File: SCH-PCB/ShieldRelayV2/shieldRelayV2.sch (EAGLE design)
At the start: 90 parts, among them IC1 LM2596SX-5.0_NOPB, IC2 LM1117MPX-33NOPB, IC3 FT231XS-R, K1 SLA-05VDC-SL-C, K2 SRD-05VDC-SL-C, K3 G3MB-202PL-DC5, K5 G3MB-202PL-DC5, K6 SRD-05VDC-SL-C, Q1 MMST2222A-7-F, Q2 MMST2222A-7-F, Q3 MMST2222A-7-F, Q4 MMST2222A-7-F, Q5 MMST2222A-7-F, Q6 MMBT3904-TP, Q7 MMBT3904-TP

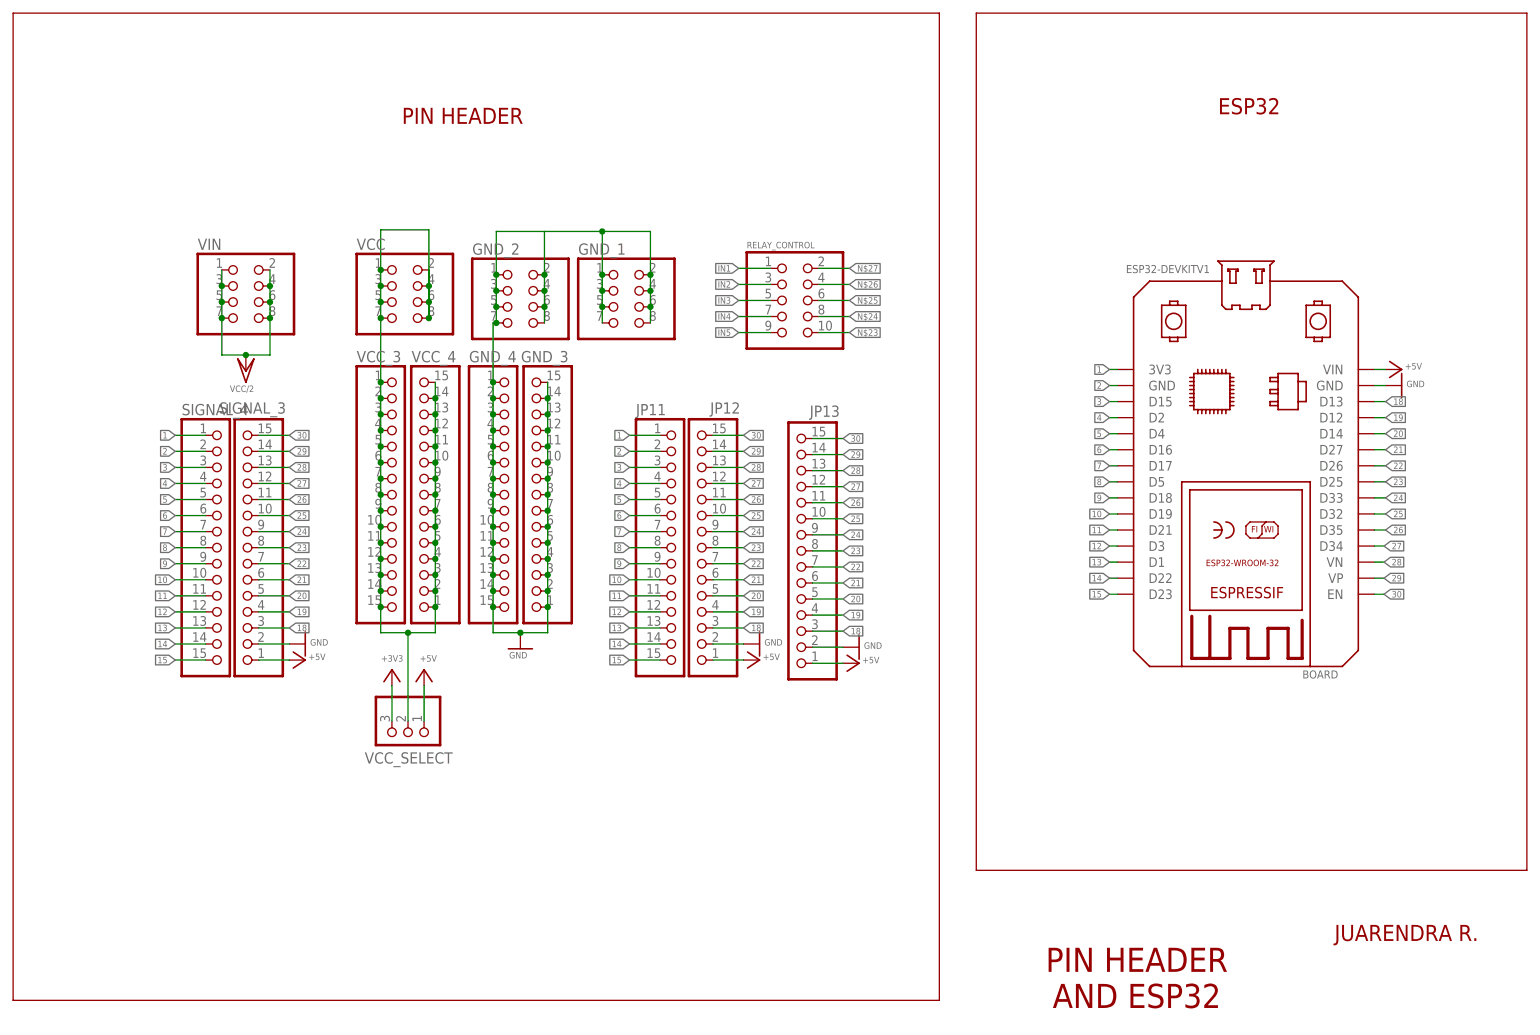
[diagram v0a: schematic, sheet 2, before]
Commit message: FEAT: update sch, board, gerber adn bom for esp embedded to pcb
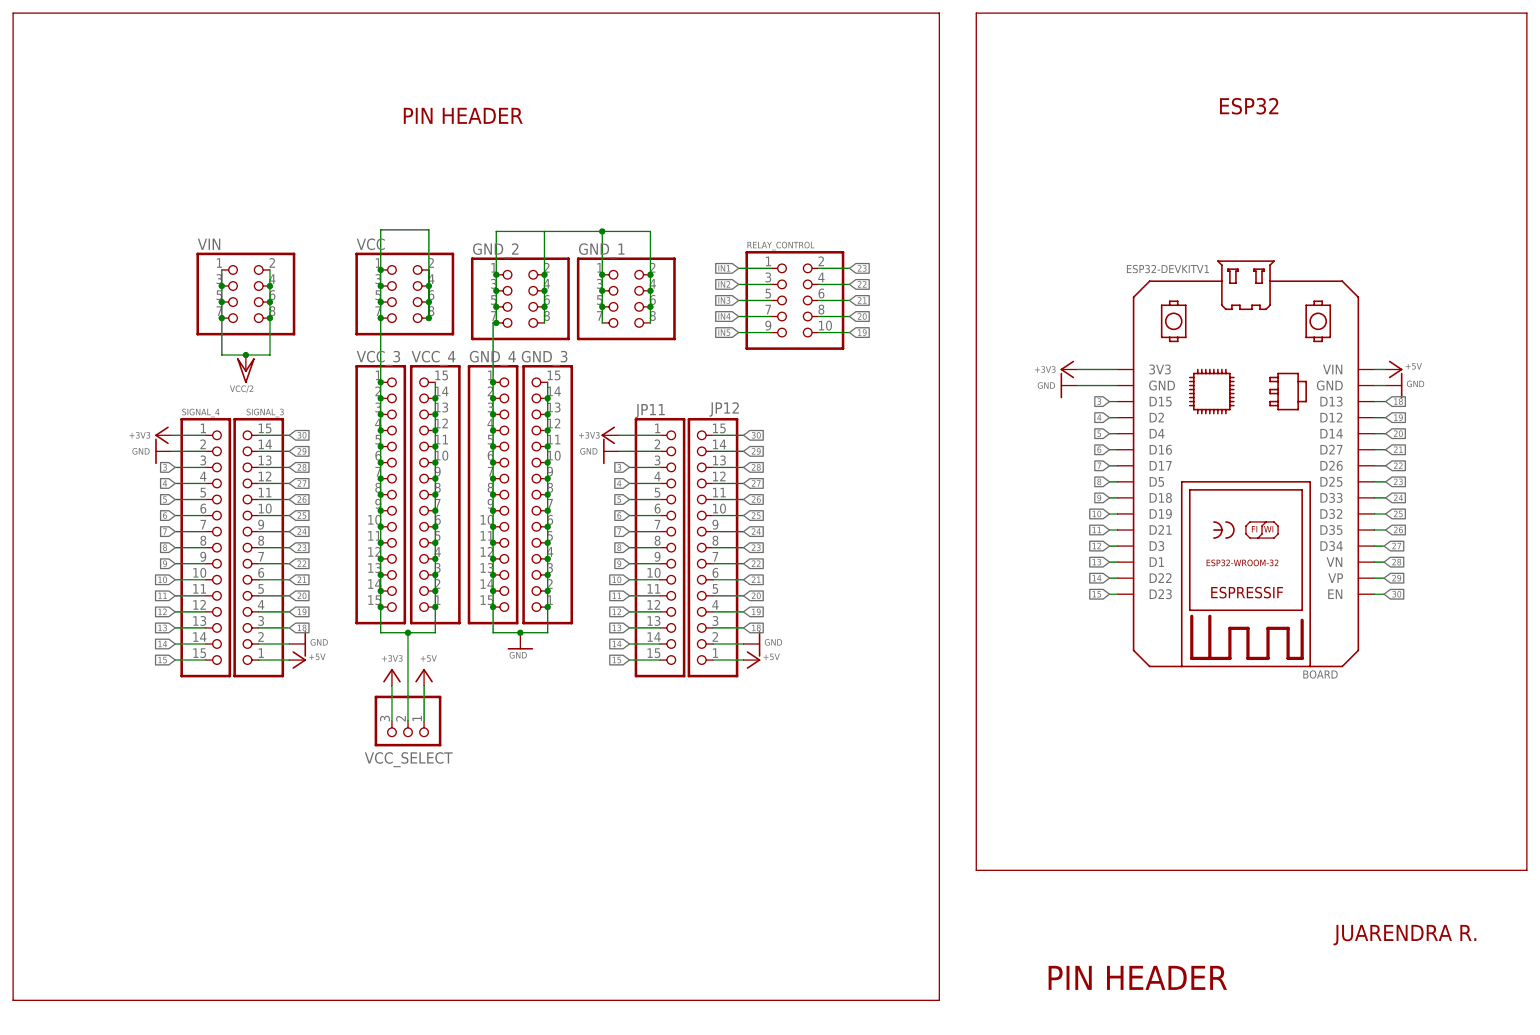
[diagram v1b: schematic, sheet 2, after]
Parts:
- removed JP13: (no value), pinhead_mod:PINHD-1X15
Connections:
- removed net 1: BOARD.3V3, JP11.1, SIGNAL_4.1
- removed net 2: BOARD.GND@1, JP11.2, SIGNAL_4.2
- removed net 3.3V: C15.2, C4.2, ESP32.3V3, LED.K, R51.1
- removed net 3V3_FTDI: IC3.VCCIO
- removed net BUTTON1: ESP32.IO18
- removed net D23: ESP32.IO23
- removed net D25: ESP32.IO25
- removed net D26: ESP32.IO26
- removed net D27: ESP32.IO27
- removed net D32: ESP32.IO32
- removed net D33: ESP32.IO33
- removed net D34: ESP32.IO34
- removed net D35: ESP32.IO35
- removed net D5: ESP32.IO5
- removed net EN: C14.P$1, ESP32.EN, Q7.C, R51.2, S1.2
- removed net LED: ESP32.IO19, R13.1
- removed net N$23: RELAY_CONTROL.10
- removed net N$24: RELAY_CONTROL.8
- removed net N$25: RELAY_CONTROL.6
- removed net N$26: RELAY_CONTROL.4
- removed net N$27: RELAY_CONTROL.2
- removed net RX_DWM: ESP32.IO17
- removed net SCL: ESP32.IO22
- removed net SDA: ESP32.IO21
- removed net SD_HOST_CLK: ESP32.IO14
- removed net SD_HOST_CMD: ESP32.IO15
- removed net SD_HOST_D0: ESP32.IO2
- removed net SD_HOST_D1: ESP32.IO4
- removed net SD_HOST_D2: ESP32.IO12
- removed net SD_HOST_D3: ESP32.IO13
- removed net TX_DWM: ESP32.IO16
- removed net U0RXD: ESP32.RXD0, IC3.TXD
- removed net U0TXD: ESP32.TXD0, IC3.RXD
- removed net VN: ESP32.SENSOR_VN
- removed net VP: ESP32.SENSOR_VP
- net +3V3: now also BOARD.3V3, C15.2, C4.2, ESP32.3V3, JP11.1, LED.K, R51.1, SIGNAL_4.1
- net +5V: no longer JP13.1
- net 10: now also ESP32.IO19
- net 11: now also ESP32.IO21
- net 12: now also ESP32.RXD0, IC3.TXD
- net 13: now also ESP32.TXD0, IC3.RXD
- net 14: now also ESP32.IO22
- net 15: now also ESP32.IO23
- net 18: now also ESP32.IO13; no longer JP13.3
- net 19: now also ESP32.IO12, RELAY_CONTROL.10; no longer JP13.4
- net 20: now also ESP32.IO14, RELAY_CONTROL.8; no longer JP13.5
- net 21: now also ESP32.IO27, RELAY_CONTROL.6; no longer JP13.6
- net 22: now also ESP32.IO26, RELAY_CONTROL.4; no longer JP13.7
- net 23: now also ESP32.IO25, RELAY_CONTROL.2; no longer JP13.8
- net 24: now also ESP32.IO33; no longer JP13.9
- net 25: now also ESP32.IO32; no longer JP13.10
- net 26: now also ESP32.IO35; no longer JP13.11
- net 27: now also ESP32.IO34; no longer JP13.12
- net 28: now also ESP32.SENSOR_VN; no longer JP13.13
- net 29: now also ESP32.SENSOR_VP; no longer JP13.14
- net 3: now also ESP32.IO15
- net 30: now also C14.P$1, ESP32.EN, Q7.C, R51.2, S1.2; no longer JP13.15
- net 3V3_OUT: now also IC3.VCCIO
- net 4: now also ESP32.IO2, R13.1
- net 5: now also ESP32.IO4
- net 6: now also ESP32.IO16
- net 7: now also ESP32.IO17
- net 8: now also ESP32.IO5
- net 9: now also ESP32.IO18
- net GND: now also BOARD.GND@1, JP11.2, SIGNAL_4.2; no longer JP13.2
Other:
- note added: "ESP and USB"
- note removed: "PIN HEADER AND ESP32"
- note removed: "SLIMEVR BY POSITRON ELEKTRONIK"

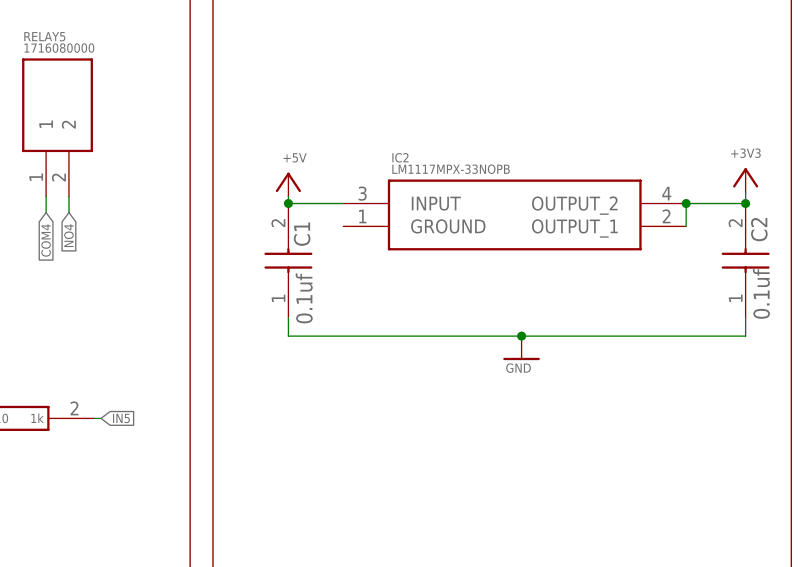
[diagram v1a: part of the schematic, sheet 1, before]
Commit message: FIX: fix gnd pin on ic 1117 that no connected
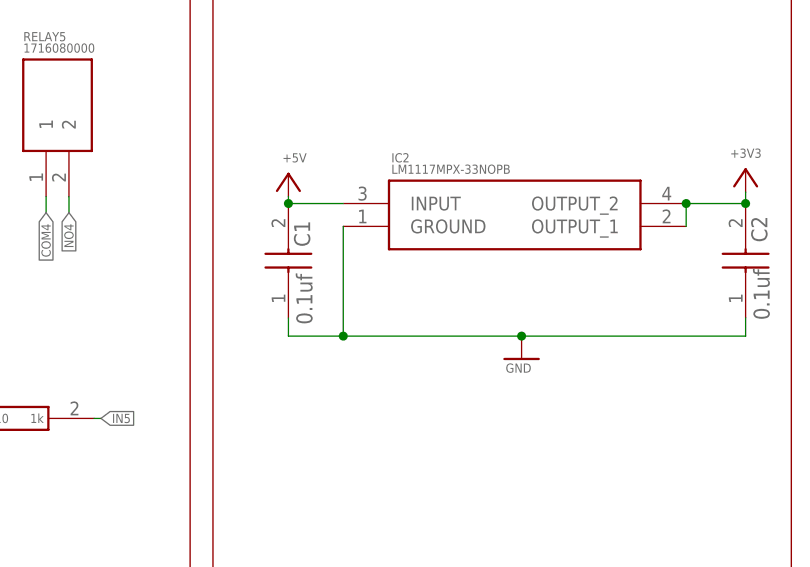
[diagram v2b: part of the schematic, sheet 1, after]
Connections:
- net GND: now also IC2.GROUND
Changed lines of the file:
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@@
 <pinref part="GND10" gate="1" pin="GND"/>
 <wire x1="196.85" y1="121.666" x2="196.85" y2="119.634" width="0.1524" layer="91"/>
-<wire x1="196.85" y1="119.634" x2="222.758" y2="119.634" width="0.1524" layer="91"/>
+<wire x1="196.85" y1="119.634" x2="202.946" y2="119.634" width="0.1524" layer="91"/>
 <pinref part="C2" gate="G$1" pin="1"/>
+<wire x1="202.946" y1="119.634" x2="222.758" y2="119.634" width="0.1524" layer="91"/>
 <wire x1="222.758" y1="119.634" x2="247.65" y2="119.634" width="0.1524" layer="91"/>
 <wire x1="247.65" y1="119.634" x2="247.65" y2="121.666" width="0.1524" layer="91"/>
 <junction x="222.758" y="119.634"/>
+<pinref part="IC2" gate="G$1" pin="GROUND"/>
+<wire x1="202.946" y1="131.826" x2="202.946" y2="119.634" width="0.1524" layer="91"/>
+<junction x="202.946" y="119.634"/>
 </segment>
 </net>

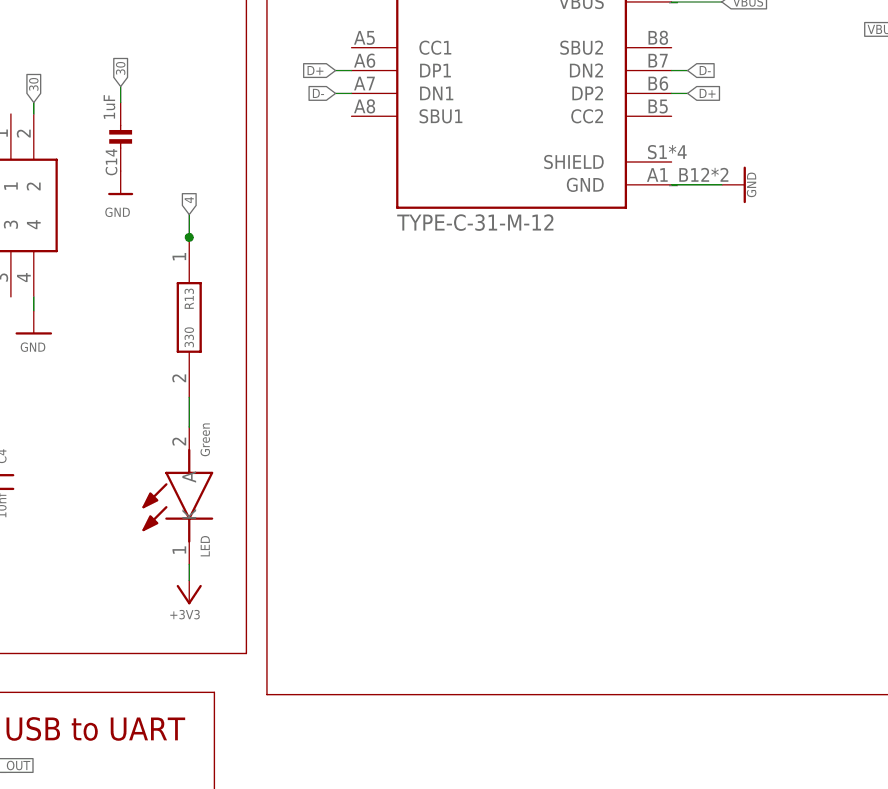
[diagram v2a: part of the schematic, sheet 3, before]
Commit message: FIX: fix led pin io2 ond katoda connected to 3v3 otherwise gns
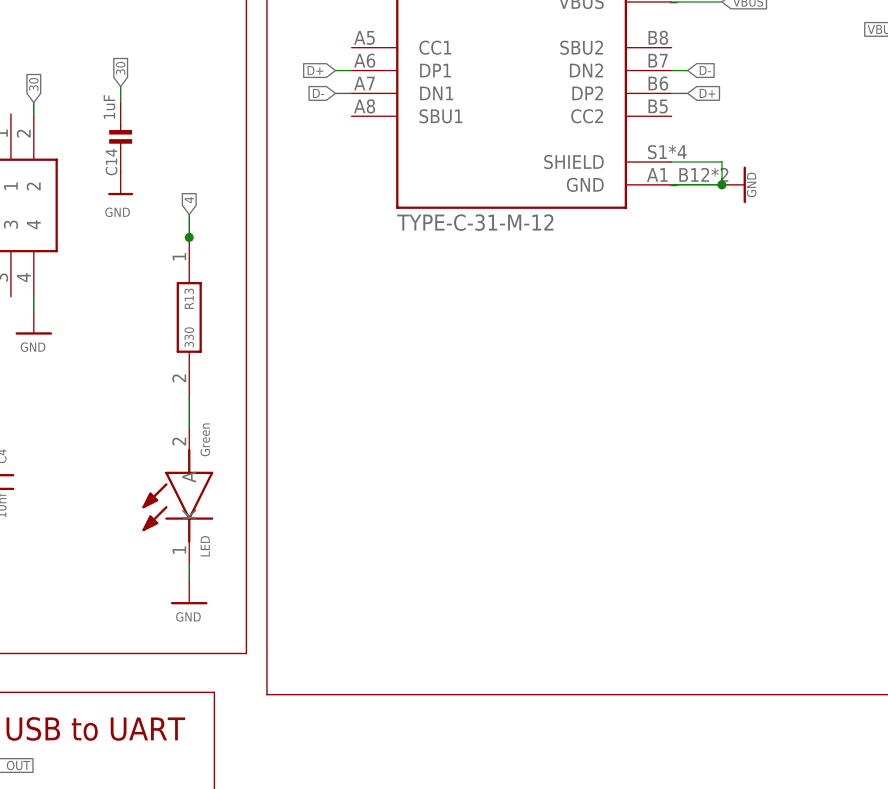
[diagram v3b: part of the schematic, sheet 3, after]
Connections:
- net +3V3: no longer LED.K
- net GND: now also LED.K, USB.SHIELD
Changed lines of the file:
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@@
 <part name="+3V5" library="supply1" library_urn="urn:adsk.eagle:library:371" deviceset="+3V3" device=""/>
 <part name="+3V6" library="supply1" library_urn="urn:adsk.eagle:library:371" deviceset="+3V3" device=""/>
-<part name="+3V7" library="supply1" library_urn="urn:adsk.eagle:library:371" deviceset="+3V3" device=""/>
 <part name="+3V8" library="supply1" library_urn="urn:adsk.eagle:library:371" deviceset="+3V3" device=""/>
 <part name="+3V9" library="supply1" library_urn="urn:adsk.eagle:library:371" deviceset="+3V3" device=""/>
+<part name="GND14" library="supply1" deviceset="GND" device=""/>
 </parts>
 <sheets>
@@
 <attribute name="VALUE" x="91.948" y="122.682" size="1.016" layer="96"/>
 </instance>
-<instance part="+3V7" gate="G$1" x="118.364" y="97.028" smashed="yes" rot="R180">
-<attribute name="VALUE" x="119.634" y="96.266" size="1.016" layer="96" rot="R180"/>
-</instance>
 <instance part="+3V8" gate="G$1" x="11.938" y="158.242" smashed="yes">
 <attribute name="VALUE" x="9.906" y="159.258" size="1.016" layer="96"/>
@@
 <instance part="+3V9" gate="G$1" x="75.946" y="159.512" smashed="yes" rot="R270">
 <attribute name="VALUE" x="76.962" y="161.544" size="1.016" layer="96" rot="R270"/>
+</instance>
+<instance part="GND14" gate="1" x="118.364" y="97.028" smashed="yes">
+<attribute name="VALUE" x="116.84" y="94.996" size="1.016" layer="96"/>
 </instance>
 </instances>
@@
 <pinref part="GND20" gate="1" pin="GND"/>
 <wire x1="171.958" y1="143.51" x2="177.546" y2="143.51" width="0.1524" layer="91"/>
+<pinref part="USB" gate="G$1" pin="SHIELD"/>
+<wire x1="171.958" y1="146.05" x2="177.546" y2="146.05" width="0.1524" layer="91"/>
+<wire x1="177.546" y1="146.05" x2="177.546" y2="143.51" width="0.1524" layer="91"/>
+<junction x="177.546" y="143.51"/>
 </segment>
 <segment>
@@
 <pinref part="GND15" gate="1" pin="GND"/>
 <wire x1="101.092" y1="131.064" x2="101.092" y2="129.54" width="0.1524" layer="91"/>
+</segment>
+<segment>
+<pinref part="LED" gate="G$1" pin="K"/>
+<wire x1="118.364" y1="101.346" x2="118.364" y2="99.568" width="0.1524" layer="91"/>
+<pinref part="GND14" gate="1" pin="GND"/>
 </segment>
 </net>
@@
 </segment>
 <segment>
-<pinref part="LED" gate="G$1" pin="K"/>
-<wire x1="118.364" y1="101.346" x2="118.364" y2="99.568" width="0.1524" layer="91"/>
-<pinref part="+3V7" gate="G$1" pin="+3V3"/>
-</segment>
-<segment>

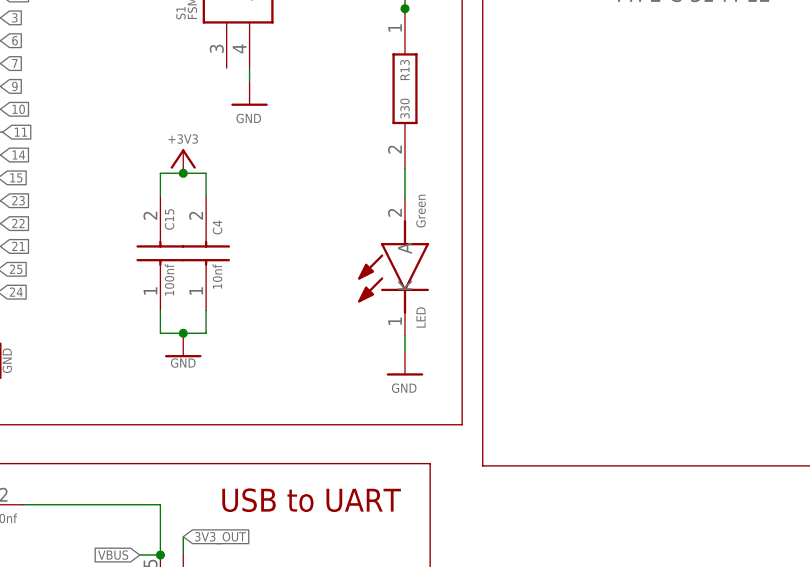
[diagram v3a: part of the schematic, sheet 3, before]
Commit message: FIX: fix led pin io2 ond katoda connected to 3v3 otherwise gns
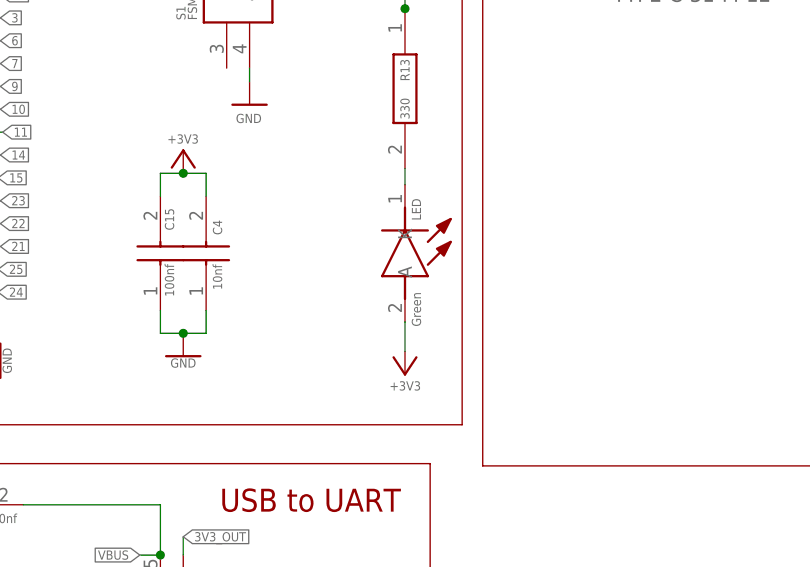
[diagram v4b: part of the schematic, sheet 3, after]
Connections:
- removed net N$34: LED.A, R13.2
- new net N$22: LED.K, R13.2
- net +3V3: now also LED.A
- net GND: no longer LED.K
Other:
- moved on the sheet: LED
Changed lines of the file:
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@@
 <part name="+3V8" library="supply1" library_urn="urn:adsk.eagle:library:371" deviceset="+3V3" device=""/>
 <part name="+3V9" library="supply1" library_urn="urn:adsk.eagle:library:371" deviceset="+3V3" device=""/>
-<part name="GND14" library="supply1" deviceset="GND" device=""/>
+<part name="+3V7" library="supply1" library_urn="urn:adsk.eagle:library:371" deviceset="+3V3" device=""/>
 </parts>
 <sheets>
@@
 <attribute name="VALUE" x="118.364" y="127.762" size="1.016" layer="96" rot="R270" align="center-left"/>
 </instance>
-<instance part="LED" gate="G$1" x="118.364" y="101.346" smashed="yes" rot="R90">
-<attribute name="NAME" x="120.65" y="102.108" size="1.016" layer="95" rot="R90"/>
-<attribute name="VALUE" x="120.65" y="113.284" size="1.016" layer="96" rot="R90"/>
+<instance part="LED" gate="G$1" x="118.364" y="118.11" smashed="yes" rot="R270">
+<attribute name="NAME" x="119.126" y="116.586" size="1.016" layer="95" rot="R270"/>
+<attribute name="VALUE" x="119.126" y="106.172" size="1.016" layer="96" rot="R270"/>
 </instance>
 <instance part="Q6" gate="G$1" x="49.276" y="40.386" smashed="yes">
@@
 <attribute name="VALUE" x="76.962" y="161.544" size="1.016" layer="96" rot="R270"/>
 </instance>
-<instance part="GND14" gate="1" x="118.364" y="97.028" smashed="yes">
-<attribute name="VALUE" x="116.84" y="94.996" size="1.016" layer="96"/>
+<instance part="+3V7" gate="G$1" x="118.364" y="97.028" smashed="yes" rot="R180">
+<attribute name="VALUE" x="120.142" y="96.266" size="1.016" layer="96" rot="R180"/>
 </instance>
 </instances>
@@
 <wire x1="101.092" y1="131.064" x2="101.092" y2="129.54" width="0.1524" layer="91"/>
 </segment>
-<segment>
-<pinref part="LED" gate="G$1" pin="K"/>
-<wire x1="118.364" y1="101.346" x2="118.364" y2="99.568" width="0.1524" layer="91"/>
-<pinref part="GND14" gate="1" pin="GND"/>
-</segment>
 </net>
 <net name="VBUS" class="0">
@@
 <wire x1="71.628" y1="136.652" x2="71.628" y2="136.656" width="0.1524" layer="91"/>
 <wire x1="71.628" y1="136.656" x2="70.788" y2="136.656" width="0.1524" layer="91"/>
-</segment>
-</net>
-<net name="N$34" class="0">
-<segment>
-<pinref part="LED" gate="G$1" pin="A"/>
-<pinref part="R13" gate="G$1" pin="2"/>
-<wire x1="118.364" y1="116.586" x2="118.364" y2="119.888" width="0.1524" layer="91"/>
 </segment>
 </net>
@@
 <pinref part="+3V9" gate="G$1" pin="+3V3"/>
 </segment>
+<segment>
+<pinref part="LED" gate="G$1" pin="A"/>
+<pinref part="+3V7" gate="G$1" pin="+3V3"/>
+<wire x1="118.364" y1="102.87" x2="118.364" y2="99.568" width="0.1524" layer="91"/>
+</segment>
 </net>
 <net name="20" class="0">
@@
 </segment>
 </net>
+<net name="N$22" class="0">
+<segment>
+<pinref part="LED" gate="G$1" pin="K"/>
+<pinref part="R13" gate="G$1" pin="2"/>
+<wire x1="118.364" y1="118.11" x2="118.364" y2="119.888" width="0.1524" layer="91"/>
+</segment>
+</net>
